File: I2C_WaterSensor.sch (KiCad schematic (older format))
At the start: 10 parts, among them J1 AVR-ISP-6, U2 ATmega328P-AU, Y1 16MHz

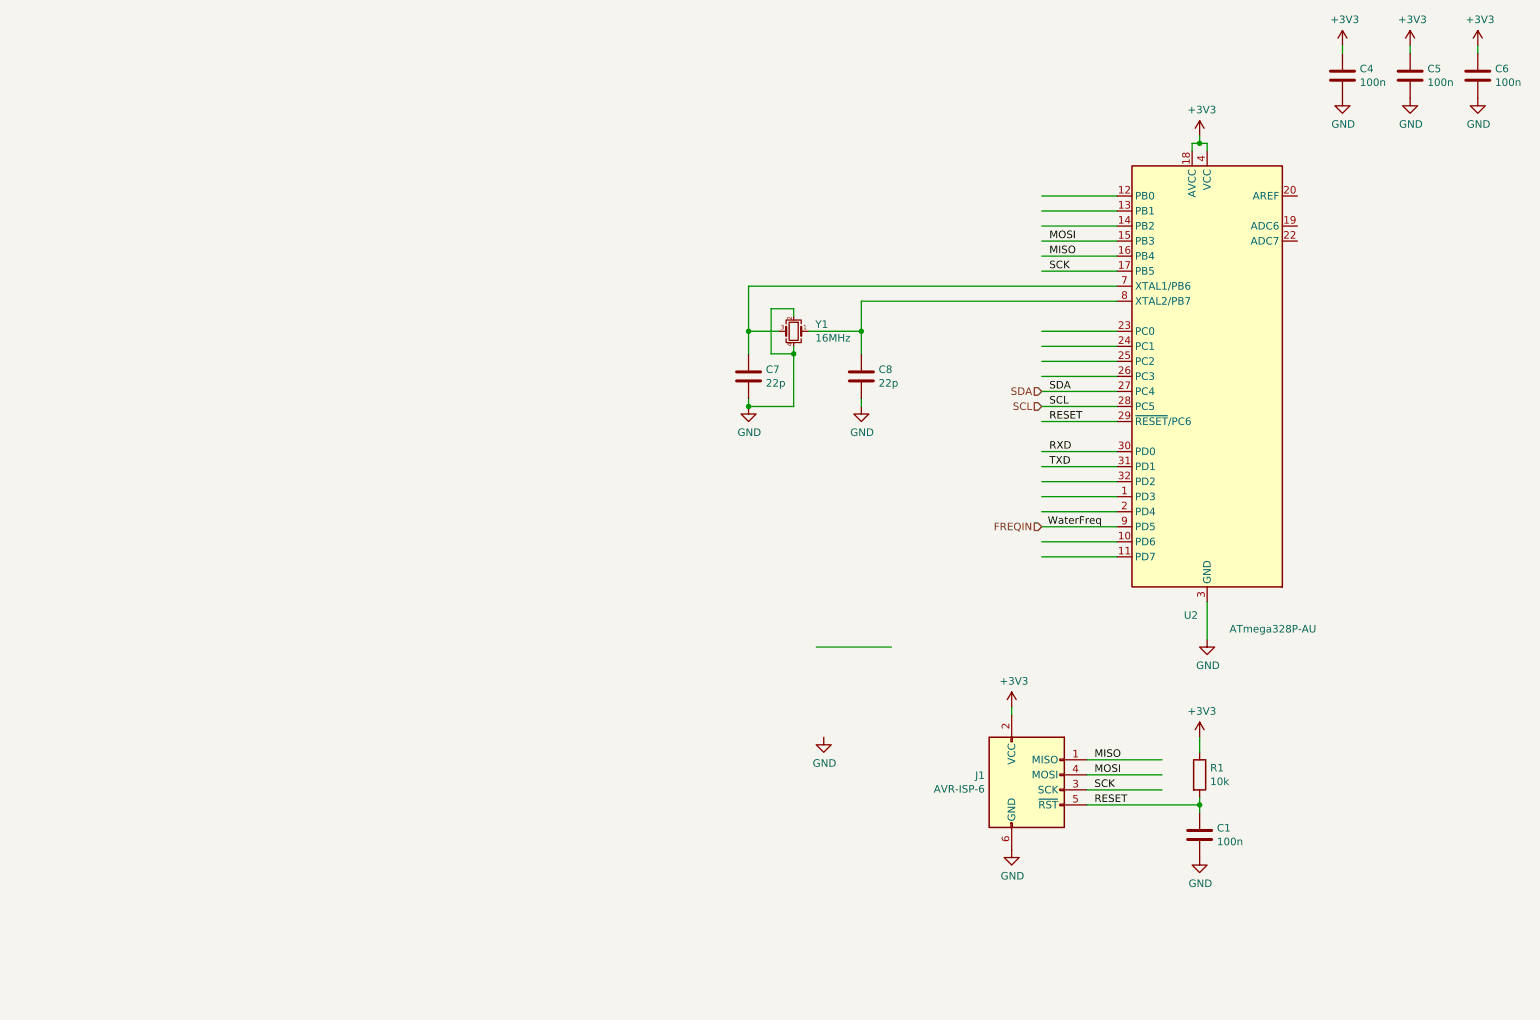
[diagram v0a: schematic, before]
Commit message: added 4-20mA input and PT100 readout
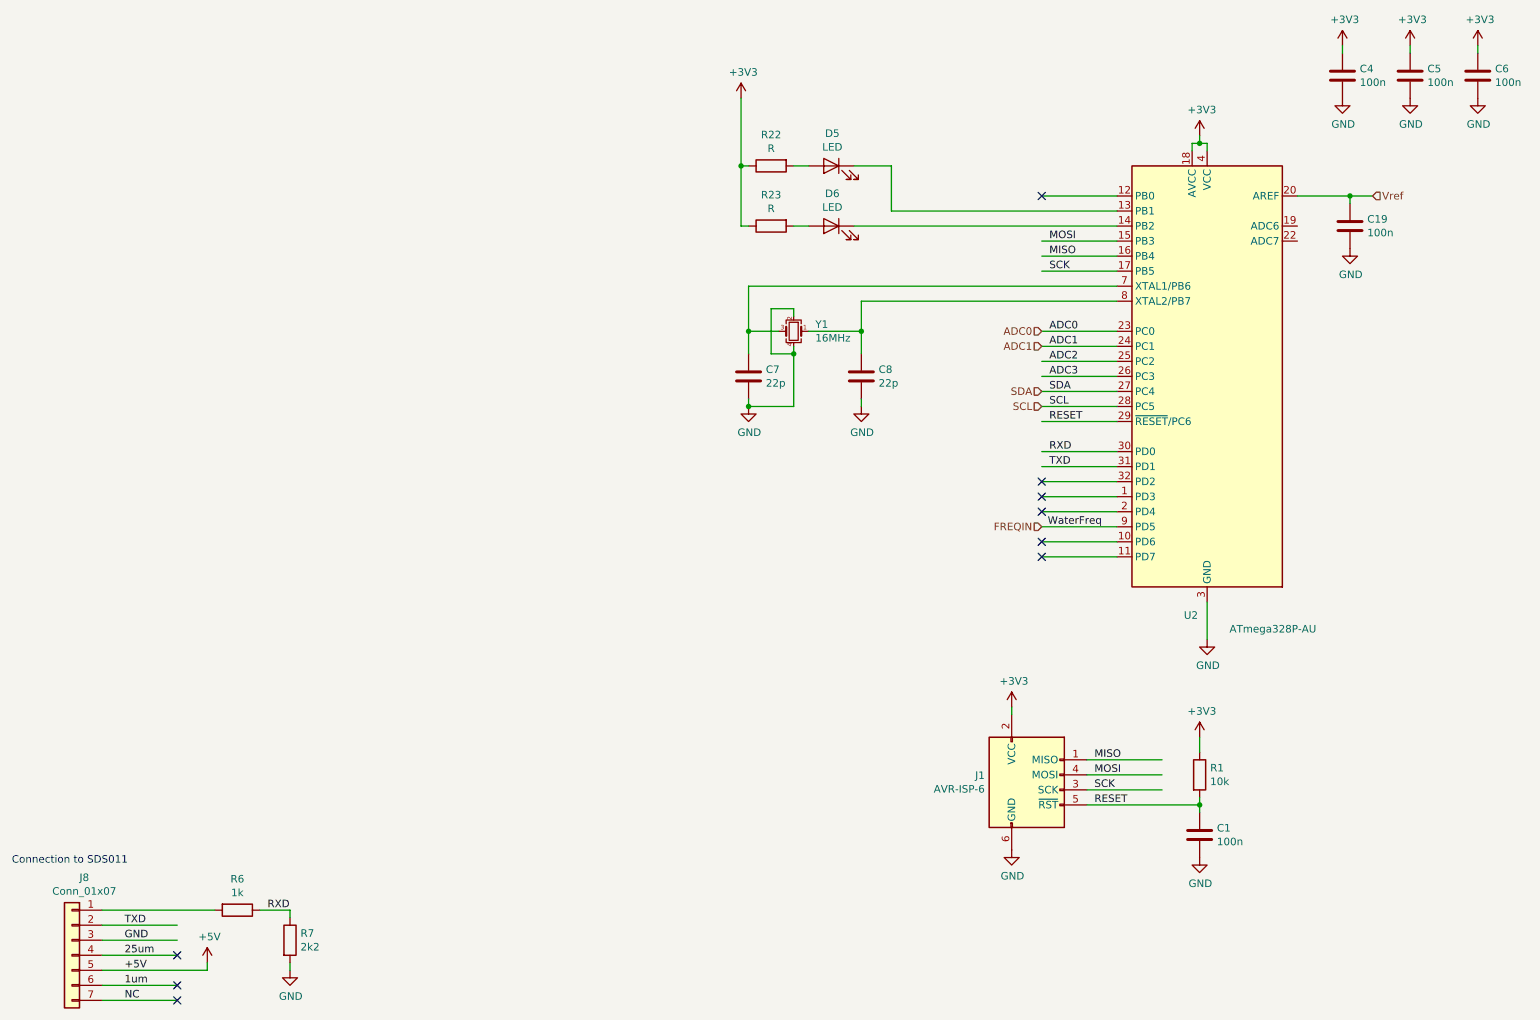
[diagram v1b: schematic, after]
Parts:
- added C19: 100n, Capacitor_SMD:C_0603_1608Metric, symbol Device:C
- added D5, D6: LED, LED_SMD:LED_0603_1608Metric, symbol Device:LED
- added J8: Conn_01x07, Connector_PinHeader_2.54mm:PinHeader_1x07_P2.54mm_Vertical, symbol Connector_Generic:Conn_01x07
- added R22, R23: R, Resistor_SMD:R_0603_1608Metric, symbol Device:R
- added R6: 1k, Resistor_SMD:R_0603_1608Metric, symbol Device:R
- added R7: 2k2, Resistor_SMD:R_0603_1608Metric, symbol Device:R
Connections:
- net labels added: +5V, 1um, 25um, ADC0, ADC1, ADC2, ADC3, NC, Vref
- wire segments 56 -> 77
- no-connect marks 0 -> 9
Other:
- note added: "Connection to SDS011"
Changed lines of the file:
@@
 $Descr A4 11693 8268
 encoding utf-8
-Sheet 2 4
+Sheet 7 7
 Title "I2C frequency sensor"
 Date ""
 Rev "1"
-Comp ""
-Comment1 "Designed for OSH Park 2 Layer Prototype"
+Comp "RWTH Aachen University, Physik 3B"
+Comment1 ""
 Comment2 ""
 Comment3 ""
@@
 Wire Wire Line
 	8000 1800 7500 1800
-Wire Wire Line
-	8000 1900 7500 1900
-Wire Wire Line
-	8000 2000 7500 2000
 Wire Wire Line
 	8000 2100 7500 2100
@@
 Text Label 7850 5850 0    50   ~ 0
 RESET
-Wire Wire Line
-	6500 4800 6000 4800
-$Comp
-L power:GND #PWR01
-U 1 1 5E7A415B
-P 6050 5400
-F 0 "#PWR01" H 6050 5150 50  0001 C CNN
-F 1 "GND" H 6055 5227 50  0000 C CNN
-F 2 "" H 6050 5400 50  0001 C CNN
-F 3 "" H 6050 5400 50  0001 C CNN
-	1    6050 5400
-	1    0    0    -1
-$EndComp
 $Comp
 L power:GND #PWR03
@@
 Connection ~ 5550 3200
 Connection ~ 5850 2850
+Text Label 7550 2700 0    50   ~ 0
+ADC0
+Text Label 7550 2800 0    50   ~ 0
+ADC1
+Text Label 7550 2900 0    50   ~ 0
+ADC2
+Text Label 7550 3000 0    50   ~ 0
+ADC3
+$Comp
+L Connector_Generic:Conn_01x07 J8
+U 1 1 5ED68C1D
+P 1050 6850
+F 0 "J8" H 968 7367 50  0000 C CNN
+F 1 "Conn_01x07" H 968 7276 50  0000 C CNN
+F 2 "Connector_PinHeader_2.54mm:PinHeader_1x07_P2.54mm_Vertical" H 1050 6850 50  0001 C CNN
+F 3 "~" H 1050 6850 50  0001 C CNN
+	1    1050 6850
+	-1   0    0    -1
+$EndComp
+Wire Wire Line
+	1750 6650 1250 6650
+Wire Wire Line
+	1750 6750 1250 6750
+Wire Wire Line
+	1750 6850 1250 6850
+Wire Wire Line
+	1750 7050 1250 7050
+Wire Wire Line
+	1750 7150 1250 7150
+Text Label 2350 6550 0    50   ~ 0
+RXD
+Text Label 1400 6650 0    50   ~ 0
+TXD
+Text Label 1400 6750 0    50   ~ 0
+GND
+Text Label 1400 6850 0    50   ~ 0
+25um
+Text Label 1400 6950 0    50   ~ 0
++5V
+Text Label 1400 7050 0    50   ~ 0
+1um
+Text Label 1400 7150 0    50   ~ 0
+NC
+Text Notes 650  6250 0    50   ~ 0
+Connection to SDS011
+$Comp
+L Device:R R6
+U 1 1 5ED771A2
+P 2150 6550
+F 0 "R6" V 1943 6550 50  0000 C CNN
+F 1 "1k" V 2034 6550 50  0000 C CNN
+F 2 "Resistor_SMD:R_0603_1608Metric" V 2080 6550 50  0001 C CNN
+F 3 "~" H 2150 6550 50  0001 C CNN
+	1    2150 6550
+	0    1    1    0
+$EndComp
+$Comp
+L Device:R R7
+U 1 1 5ED783E0
+P 2500 6750
+F 0 "R7" H 2570 6796 50  0000 L CNN
+F 1 "2k2" H 2570 6705 50  0000 L CNN
+F 2 "Resistor_SMD:R_0603_1608Metric" V 2430 6750 50  0001 C CNN
+F 3 "~" H 2500 6750 50  0001 C CNN
+	1    2500 6750
+	1    0    0    -1
+$EndComp
+Wire Wire Line
+	2300 6550 2500 6550
+Wire Wire Line
+	2500 6550 2500 6600
+$Comp
+L power:GND #PWR039
+U 1 1 5ED7CF1F
+P 2500 6950
+F 0 "#PWR039" H 2500 6700 50  0001 C CNN
+F 1 "GND" H 2505 6777 50  0000 C CNN
+F 2 "" H 2500 6950 50  0001 C CNN
+F 3 "" H 2500 6950 50  0001 C CNN
+	1    2500 6950
+	1    0    0    -1
+$EndComp
+Wire Wire Line
+	1950 6950 1950 6900
+Wire Wire Line
+	1250 6950 1950 6950
+$Comp
+L power:+5V #PWR038
+U 1 1 5ED7D826
+P 1950 6900
+F 0 "#PWR038" H 1950 6750 50  0001 C CNN
+F 1 "+5V" H 1965 7073 50  0000 C CNN
+F 2 "" H 1950 6900 50  0001 C CNN
+F 3 "" H 1950 6900 50  0001 C CNN
+	1    1950 6900
+	1    0    0    -1
+$EndComp
+Text HLabel 7500 2700 0    50   Input ~ 0
+ADC0
+Text HLabel 7500 2800 0    50   Input ~ 0
+ADC1
+Wire Wire Line
+	2500 6950 2500 6900
+Wire Wire Line
+	1250 6550 2000 6550
+NoConn ~ 7500 3700
+NoConn ~ 7500 3800
+NoConn ~ 7500 3900
+NoConn ~ 7500 4100
+NoConn ~ 7500 4200
+NoConn ~ 7500 1800
+NoConn ~ 1750 7150
+NoConn ~ 1750 7050
+NoConn ~ 1750 6850
+Text HLabel 9700 1800 2    50   Input ~ 0
+Vref
+Wire Wire Line
+	9700 1800 9550 1800
+$Comp
+L Device:C C19
+U 1 1 5EEC80F6
+P 9550 2000
+F 0 "C19" H 9665 2046 50  0000 L CNN
+F 1 "100n" H 9665 1955 50  0000 L CNN
+F 2 "Capacitor_SMD:C_0603_1608Metric" H 9588 1850 50  0001 C CNN
+F 3 "~" H 9550 2000 50  0001 C CNN
+	1    9550 2000
+	1    0    0    -1
+$EndComp
+$Comp
+L power:GND #PWR062
+U 1 1 5EEC80FC
+P 9550 2150
+F 0 "#PWR062" H 9550 1900 50  0001 C CNN
+F 1 "GND" H 9555 1977 50  0000 C CNN
+F 2 "" H 9550 2150 50  0001 C CNN
+F 3 "" H 9550 2150 50  0001 C CNN
+	1    9550 2150
+	1    0    0    -1
+$EndComp
+Wire Wire Line
+	9550 1850 9550 1800
+Connection ~ 9550 1800
+Wire Wire Line
+	9550 1800 9200 1800
+$Comp
+L Device:LED D5
+U 1 1 5EED8A11
+P 6100 1600
+F 0 "D5" H 6093 1816 50  0000 C CNN
+F 1 "LED" H 6093 1725 50  0000 C CNN
+F 2 "LED_SMD:LED_0603_1608Metric" H 6100 1600 50  0001 C CNN
+F 3 "~" H 6100 1600 50  0001 C CNN
+	1    6100 1600
+	-1   0    0    -1
+$EndComp
+$Comp
+L Device:LED D6
+U 1 1 5EEDA40A
+P 6100 2000
+F 0 "D6" H 6093 2216 50  0000 C CNN
+F 1 "LED" H 6093 2125 50  0000 C CNN
+F 2 "LED_SMD:LED_0603_1608Metric" H 6100 2000 50  0001 C CNN
+F 3 "~" H 6100 2000 50  0001 C CNN
+	1    6100 2000
+	-1   0    0    -1
+$EndComp
+$Comp
+L Device:R R22
+U 1 1 5EEDC07F
+P 5700 1600
+F 0 "R22" V 5493 1600 50  0000 C CNN
+F 1 "R" V 5584 1600 50  0000 C CNN
+F 2 "Resistor_SMD:R_0603_1608Metric" V 5630 1600 50  0001 C CNN
+F 3 "~" H 5700 1600 50  0001 C CNN
+	1    5700 1600
+	0    -1   1    0
+$EndComp
+$Comp
+L Device:R R23
+U 1 1 5EEDC80F
+P 5700 2000
+F 0 "R23" V 5493 2000 50  0000 C CNN
+F 1 "R" V 5584 2000 50  0000 C CNN
+F 2 "Resistor_SMD:R_0603_1608Metric" V 5630 2000 50  0001 C CNN
+F 3 "~" H 5700 2000 50  0001 C CNN
+	1    5700 2000
+	0    -1   1    0
+$EndComp
+Wire Wire Line
+	5850 1600 5950 1600
+Wire Wire Line
+	5850 2000 5950 2000
+Wire Wire Line
+	8000 1900 6500 1900
+Wire Wire Line
+	6500 1900 6500 1600
+Wire Wire Line
+	6500 1600 6250 1600
+Wire Wire Line
+	8000 2000 6250 2000
+Wire Wire Line
+	5550 2000 5500 2000
+Wire Wire Line
+	5500 2000 5500 1600
+Wire Wire Line
+	5550 1600 5500 1600
+Connection ~ 5500 1600
+$Comp
+L power:+3V3 #PWR063
+U 1 1 5EEF3C31
+P 5500 1150
+F 0 "#PWR063" H 5500 1000 50  0001 C CNN
+F 1 "+3V3" H 5515 1323 50  0000 C CNN
+F 2 "" H 5500 1150 50  0001 C CNN
+F 3 "" H 5500 1150 50  0001 C CNN
+	1    5500 1150
+	1    0    0    -1
+$EndComp
+Wire Wire Line
+	5500 1150 5500 1600
 $EndSCHEMATC

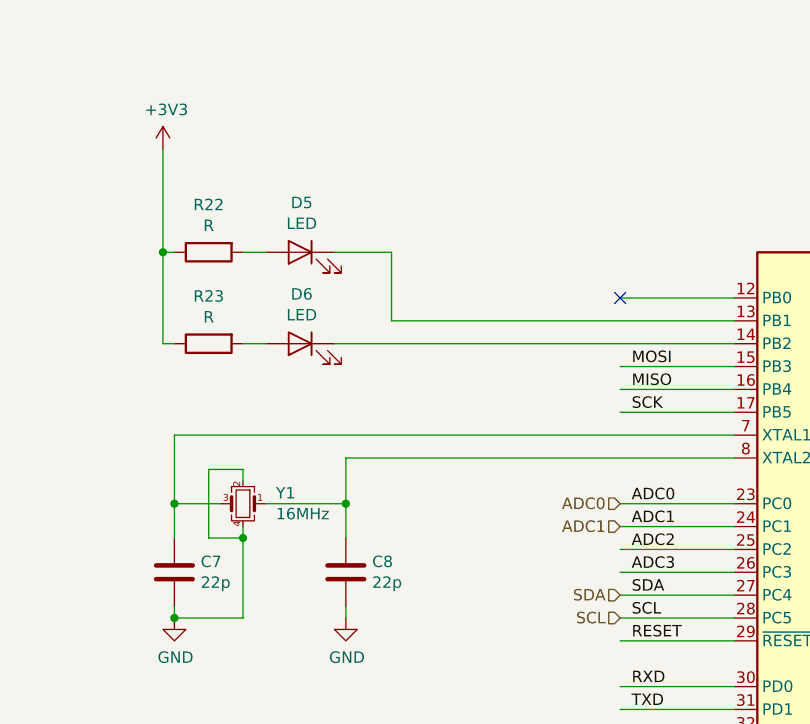
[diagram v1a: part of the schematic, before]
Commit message: added BPW34 for measurement of light intensity
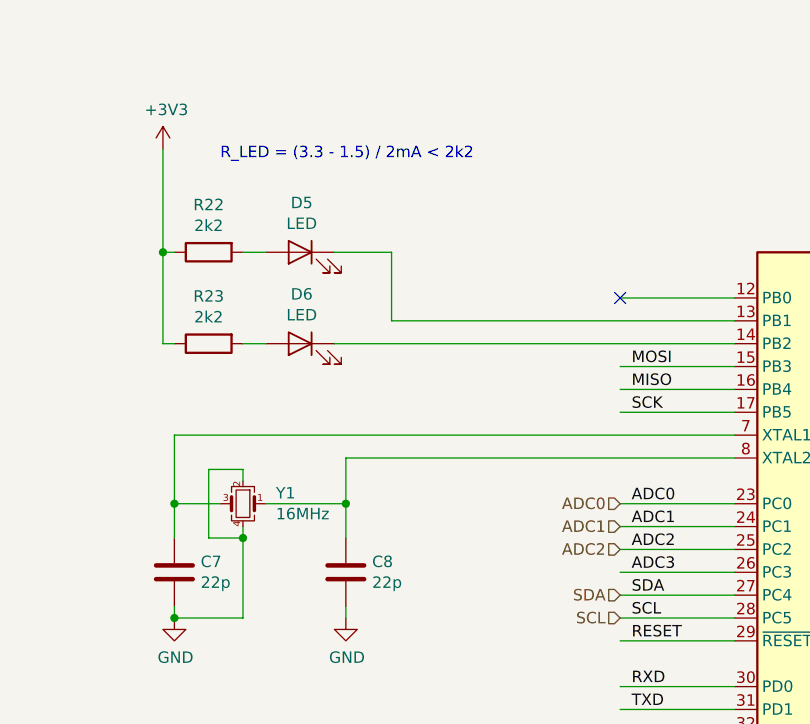
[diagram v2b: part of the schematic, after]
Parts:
- R22, R23: value R -> 2k2
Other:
- note added: "R_LED = (3.3 - 1.5) / 2mA < 2k2"
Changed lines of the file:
@@
 P 5700 1600
 F 0 "R22" V 5493 1600 50  0000 C CNN
-F 1 "R" V 5584 1600 50  0000 C CNN
+F 1 "2k2" V 5584 1600 50  0000 C CNN
 F 2 "Resistor_SMD:R_0603_1608Metric" V 5630 1600 50  0001 C CNN
 F 3 "~" H 5700 1600 50  0001 C CNN
@@
 P 5700 2000
 F 0 "R23" V 5493 2000 50  0000 C CNN
-F 1 "R" V 5584 2000 50  0000 C CNN
+F 1 "2k2" V 5584 2000 50  0000 C CNN
 F 2 "Resistor_SMD:R_0603_1608Metric" V 5630 2000 50  0001 C CNN
 F 3 "~" H 5700 2000 50  0001 C CNN
@@
 Wire Wire Line
 	5500 1150 5500 1600
+Text HLabel 7500 2900 0    50   Input ~ 0
+ADC2
+Text Notes 5750 1200 0    50   ~ 0
+R_LED = (3.3 - 1.5) / 2mA < 2k2
 $EndSCHEMATC

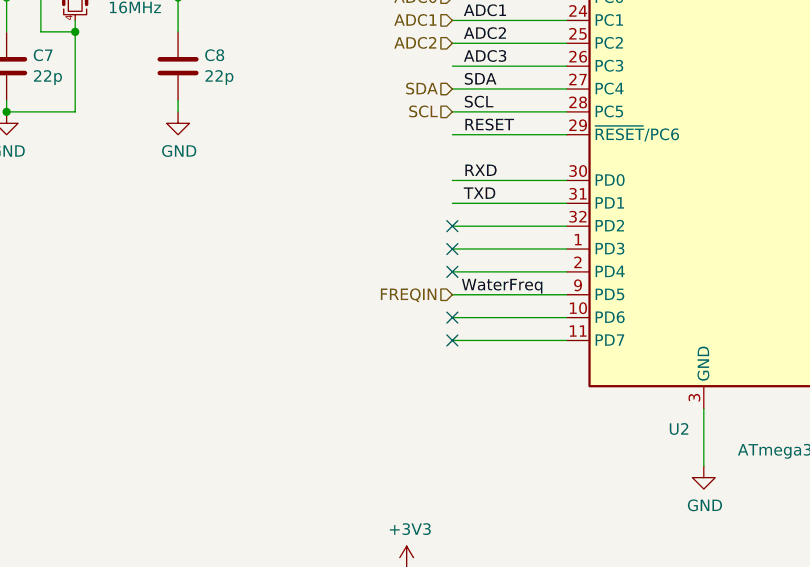
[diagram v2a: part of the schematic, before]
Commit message: added digital output, 24V to 5V voltage regulator
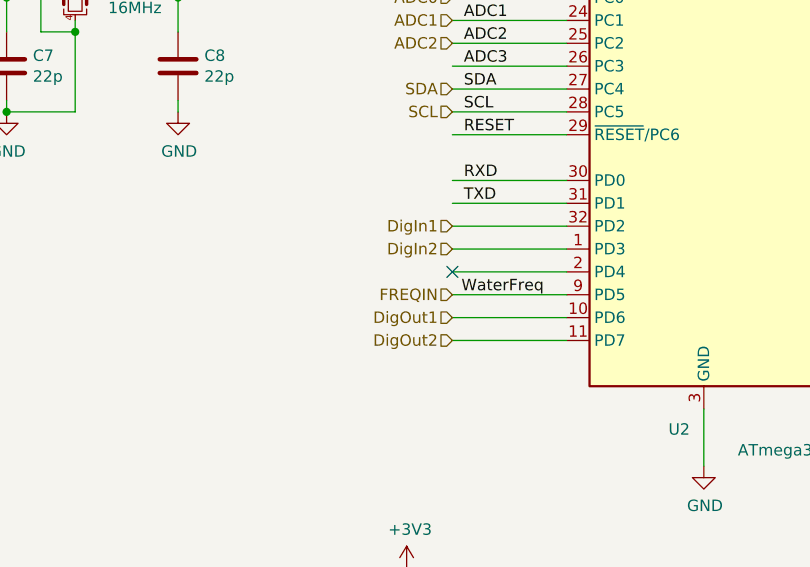
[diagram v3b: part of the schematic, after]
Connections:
- net labels added: DigIn1, DigIn2, DigOut1, DigOut2
- no-connect marks 9 -> 5
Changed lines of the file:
@@
 Wire Wire Line
 	1250 6550 2000 6550
-NoConn ~ 7500 3700
-NoConn ~ 7500 3800
 NoConn ~ 7500 3900
-NoConn ~ 7500 4100
-NoConn ~ 7500 4200
 NoConn ~ 7500 1800
 NoConn ~ 1750 7150
@@
 Text Notes 5750 1200 0    50   ~ 0
 R_LED = (3.3 - 1.5) / 2mA < 2k2
+Text HLabel 7500 4100 0    50   Input ~ 0
+DigOut1
+Text HLabel 7500 4200 0    50   Input ~ 0
+DigOut2
+Text HLabel 7500 3700 0    50   Input ~ 0
+DigIn1
+Text HLabel 7500 3800 0    50   Input ~ 0
+DigIn2
 $EndSCHEMATC
